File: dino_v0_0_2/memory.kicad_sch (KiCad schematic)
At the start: 10 parts, among them U19 74LS245, U21 74LS245, U24 AT28C256, U26 MCM60256AP, U51 7400

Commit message: fix(schematic): declare matching label sets so aliased nets stay one net
Three board-to-board wires were absent from the generated continuity
checklist, which is the only coverage the netlist->copper step has. A wire
missing from that list is driven by no test and sampled by no test -- the
MAR-lo post-mortem in one sentence.

Cause: cross-sheet connectivity in this design is a naming convention (all
labels are sheet-local; KiCad joins nothing between sheets). kicad_netlist
keys a net on its full label set, joined. When one sheet carries an alias and
another doesn't, the same physical wire gets two keys, both look single-sheet,
and continuity_checklist's cross-sheet filter drops the whole net.

    M15/ROM_EN   mar had both labels, memory had only ROM_EN (on a stub that
                 never joined U24.20's wire), program_counter had only M15.
                 The ROM chip-enable. Missing from every checklist ever
                 generated; survived only because a dead ~CE means the machine
                 never boots, so it self-reports.
    CW17 / CW18  microcode had the bare names, control_word had both. These
                 are U23's only wired outputs -- the entire bank-1 feature
                 rides on them, and both decoders lose their enable if either
                 is unlanded, which at the bench reads like a bad ROM burn.

Fix is in the schematic, not the tool: every sheet touching an aliased net now
declares the same label set. Alias ordering already satisfied the CWnn rule
(`~` sorts after `C`), so CW17/CW18 stay canonical and stay bus members.

  memory           U24.20  ROM_EN -> M15/ROM_EN
  program_counter  U12.9   M15    -> M15/ROM_EN
                   U14.9   M15    -> M15/ROM_EN
  microcode        U23.12  CW17   -> CW17/~{SRC_BANK}
                   U23.13  CW18   -> CW18/~{DST_BANK}

stack_pointer.kicad_sch is UUID churn only, zero connectivity change: the
sheet shipped with 14 duplicate UUIDs (one repeated 5x, consistent with the
four 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
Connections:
- net ROM_EN is gone; now on net M15: U24.20 (~{CE})
- no-connect marks 3 -> 1
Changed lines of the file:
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@@
 		(at 93.98 27.94)
-	)
-	(no_connect
-		(at 245.11 115.57)
-	)
-	(no_connect
-		(at 57.15 115.57)
 	)
 	(bus_entry
@@
 	(wire
 		(pts
+			(xy 245.11 115.57) (xy 245.11 118.11)
+		)
+		(stroke
+			(width 0)
+			(type default)
+		)
+	)
+	(wire
+		(pts
 			(xy 34.29 182.88) (xy 29.21 182.88)
 		)
@@
 		(pts
 			(xy 168.91 63.5) (xy 153.67 63.5)
+		)
+		(stroke
+			(width 0)
+			(type default)
+		)
+	)
+	(wire
+		(pts
+			(xy 57.15 115.57) (xy 57.15 118.11)
 		)
 		(stroke
@@
 		)
 	)
+	(label "ROM_EN"
+		(at 245.11 118.11 180)
+		(effects
+			(font
+				(size 1.27 1.27)
+			)
+			(justify right bottom)
+		)
+	)
 	(label "MDR7"
 		(at 148.59 76.2 180)
@@
 		)
 	)
+	(label "ROM_EN"
+		(at 57.15 118.11 0)
+		(effects
+			(font
+				(size 1.27 1.27)
+			)
+			(justify left bottom)
+		)
+	)

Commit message: feat: phase D on silicon — the machine executes from RAM
PROG_ramexec returns 0x6E. The PC has been above 0x7FFF and FETCH_RAM has
been high, both for the first time in this machine's life.

The missing condition was never "is this a fetch." ~ROM_OUT is asserted for
every src=ROM — opcode fetch, LDAI's immediate, LDA/STA/JMP/CALL operand
bytes — so an instruction living in RAM must read its operands from RAM
too. The condition is "a ROM-side read was requested, but the address is
above 0x7FFF":

    FETCH_RAM = NOR(~ROM_OUT, ~RAM_EN)

Six gate sections, no new IC. All six were free on U22/U37/U39, already in
sockets on the MDR board, where ~ROM_OUT and ~RAM_OUT already sit feeding
READS_IDLE. Only ~RAM_EN had to be brought in.

    U22 g3   FETCH_RAM     = NOR(~ROM_OUT, ~RAM_EN)
    U22 g4   ROM_BUF_ON    = NOR(~ROM_OUT, FETCH_RAM)
    U37 inv4 ~{FETCH_RAM}
    U37 inv6 ~{ROM_BUF_EN} = OR(~ROM_OUT, FETCH_RAM)   -> U19.19
    U37 inv5 ~{RAM_OE_G}   = AND(~RAM_OUT, ~FETCH_RAM) -> U26.22 + U51.9
    U39 g4   RAM_OE_ON     = NAND(~RAM_OUT, ~FETCH_RAM)

Two pin lifts on the memory board, eleven wires. U24.22 stays on ~ROM_OUT:
U24's own ~CE = M15 already deselects the ROM chip at RAM addresses.

Gating ~RAM_OUT upstream is what keeps this at six gates rather than eight.
U51 is a 7400 computing ~RAM_MDR_EN = AND(~RAM_OUT, ~WRITE_DIR), so one
gate on ~RAM_OUT moves both the RAM chip's ~OE and its buffer's ~CE.

Re-proved before building: all 15 src=ROM microcode rows carry mux_pc=True,
FETCH included, and FILL is src=NONE. A ROM-side read can now land in RAM,
so the standing "ROM reads are exempt from the src=RAM -> MAR loop" rule was
no longer free. It holds — MAR never drives M during a ROM-side read, and a
runaway opcode cannot open the loop either.

The witness is not permutation-blind. If the fetch had still come from ROM,
PC=0x9000 presents A0-A14 = 0x1000 to U24, which is 0xFF fill, which is
HALT, so the poison would have survived as 0xFF. 0x6E is 0x8B - 0x1D,
compu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
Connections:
- net ~{ROM_OUT}: no longer U19.19 (CE)
- net ~{RAM_OUT} renamed ~{RAM_OE_G}
- new net ~{ROM_BUF_EN}: U19.19 (CE)
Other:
- note added: "MODULE CONTRACT — generated, do not hand-edit (kicad_contracts.py --stamp) IN: ~{ROM_OUT} <- Control Word Module IN: ~{RAM_EN} <- Memory Address Regiser IN: M0-14, M15=ROM_EN <- Memory Address Regiser, Program Counter IN: WRITE_DIR, ~{RAM_OE_G}, ~{ROM_BUF_EN} <- Memory Data Register IN: ~{CLK} <- root OUT: MDR0-7 -> Memory Data Register, Register Modules, Stack Pointer"
- note removed: "MODULE CONTRACT — generated, do not hand-edit (kicad_contracts.py --stamp) IN: ~{RAM_OUT}, ~{ROM_OUT} <- Control Word Module IN: ~{RAM_EN} <- Memory Address Regiser IN: M0-14, M15=ROM_EN <- Memory Address Regiser, Program Counter IN: WRITE_DIR <- Memory Data Register IN: ~{CLK} <- root OUT: MDR0-7 -> Memory Data Register, Register Modules"
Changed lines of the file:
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@@
 		)
 	)
-	(text "MODULE CONTRACT — generated, do not hand-edit (kicad_contracts.py --stamp)\nIN: ~{RAM_OUT}, ~{ROM_OUT} <- Control Word Module\nIN: ~{RAM_EN} <- Memory Address Regiser\nIN: M0-14, M15=ROM_EN <- Memory Address Regiser, Program Counter\nIN: WRITE_DIR <- Memory Data Register\nIN: ~{CLK} <- root\nOUT: MDR0-7 -> Memory Data Register, Register Modules"
-		(exclude_from_sim no)
-		(at 160.02 165.1 0)
-		(effects
-			(font
-				(size 1.27 1.27)
-			)
-			(justify left bottom)
-		)
-	)
 	(text "ROM"
 		(exclude_from_sim no)
@@
 	)
 	(junction
-		(at 194.31 104.14)
-		(diameter 0)
-		(color 0 0 0 0)
-	)
-	(junction
 		(at 96.52 40.64)
 		(diameter 0)
@@
 	(wire
 		(pts
-			(xy 194.31 104.14) (xy 194.31 111.76)
-		)
-		(stroke
-			(width 0)
-			(type default)
-		)
-	)
-	(wire
-		(pts
 			(xy 109.22 83.82) (xy 104.14 83.82)
 		)
@@
 	(wire
 		(pts
-			(xy 190.5 104.14) (xy 194.31 104.14)
+			(xy 190.5 110.49) (xy 194.31 110.49)
 		)
 		(stroke
@@
 	(wire
 		(pts
-			(xy 194.31 83.82) (xy 194.31 104.14)
-		)
-		(stroke
-			(width 0)
-			(type default)
-		)
-	)
-	(wire
-		(pts
 			(xy 204.47 73.66) (xy 194.31 73.66)
 		)
@@
 		)
 	)
+	(wire
+		(pts
+			(xy 194.31 110.49) (xy 194.31 111.76)
+		)
+		(stroke
+			(width 0)
+			(type default)
+		)
+	)
 	(bus
 		(pts
@@
 	(wire
 		(pts
+			(xy 190.5 105.41) (xy 194.31 105.41)
+		)
+		(stroke
+			(width 0)
+			(type default)
+		)
+	)
+	(wire
+		(pts
 			(xy 97.79 73.66) (xy 97.79 68.58)
 		)
@@
 		)
 	)
+	(wire
+		(pts
+			(xy 194.31 83.82) (xy 194.31 105.41)
+		)
+		(stroke
+			(width 0)
+			(type default)
+		)
+	)
 	(label "M0"
 		(at 245.11 58.42 180)
@@
 		)
 	)
-	(label "~{RAM_OUT}"
+	(label "~{RAM_OE_G}"
 		(at 116.84 99.06 0)
 		(effects
@@
 	)
 	(label "~{ROM_OUT}"
-		(at 190.5 104.14 180)
+		(at 190.5 110.49 180)
 		(effects
 			(font
@@
 		)
 	)
+	(label "~{ROM_BUF_EN}"
+		(at 190.5 105.41 180)
+		(effects
+			(font
+				(size 1.27 1.27)
+			)
+			(justify right bottom)
+		)
+	)
 	(label "WRITE_DIR"
 		(at 35.56 142.24 180)
@@
 		)
 	)
-	(label "~{RAM_OUT}"
+	(label "~{RAM_OE_G}"
 		(at 29.21 182.88 180)
 		(effects
@@
 		)
 	)
+	(text "MODULE CONTRACT — generated, do not hand-edit (kicad_contracts.py --stamp)\nIN: ~{ROM_OUT} <- Control Word Module\nIN: ~{RAM_EN} <- Memory Address Regiser\nIN: M0-14, M15=ROM_EN <- Memory Address Regiser, Program Counter\nIN: WRITE_DIR, ~{RAM_OE_G}, ~{ROM_BUF_EN} <- Memory Data Register\nIN: ~{CLK} <- root\nOUT: MDR0-7 -> Memory Data Register, Register Modules, Stack Pointer"
+		(exclude_from_sim no)
+		(at 160.02 165.1 0)
+		(effects
+			(font
+				(size 1.27 1.27)
+			)
+			(justify left bottom)
+		)
+	)

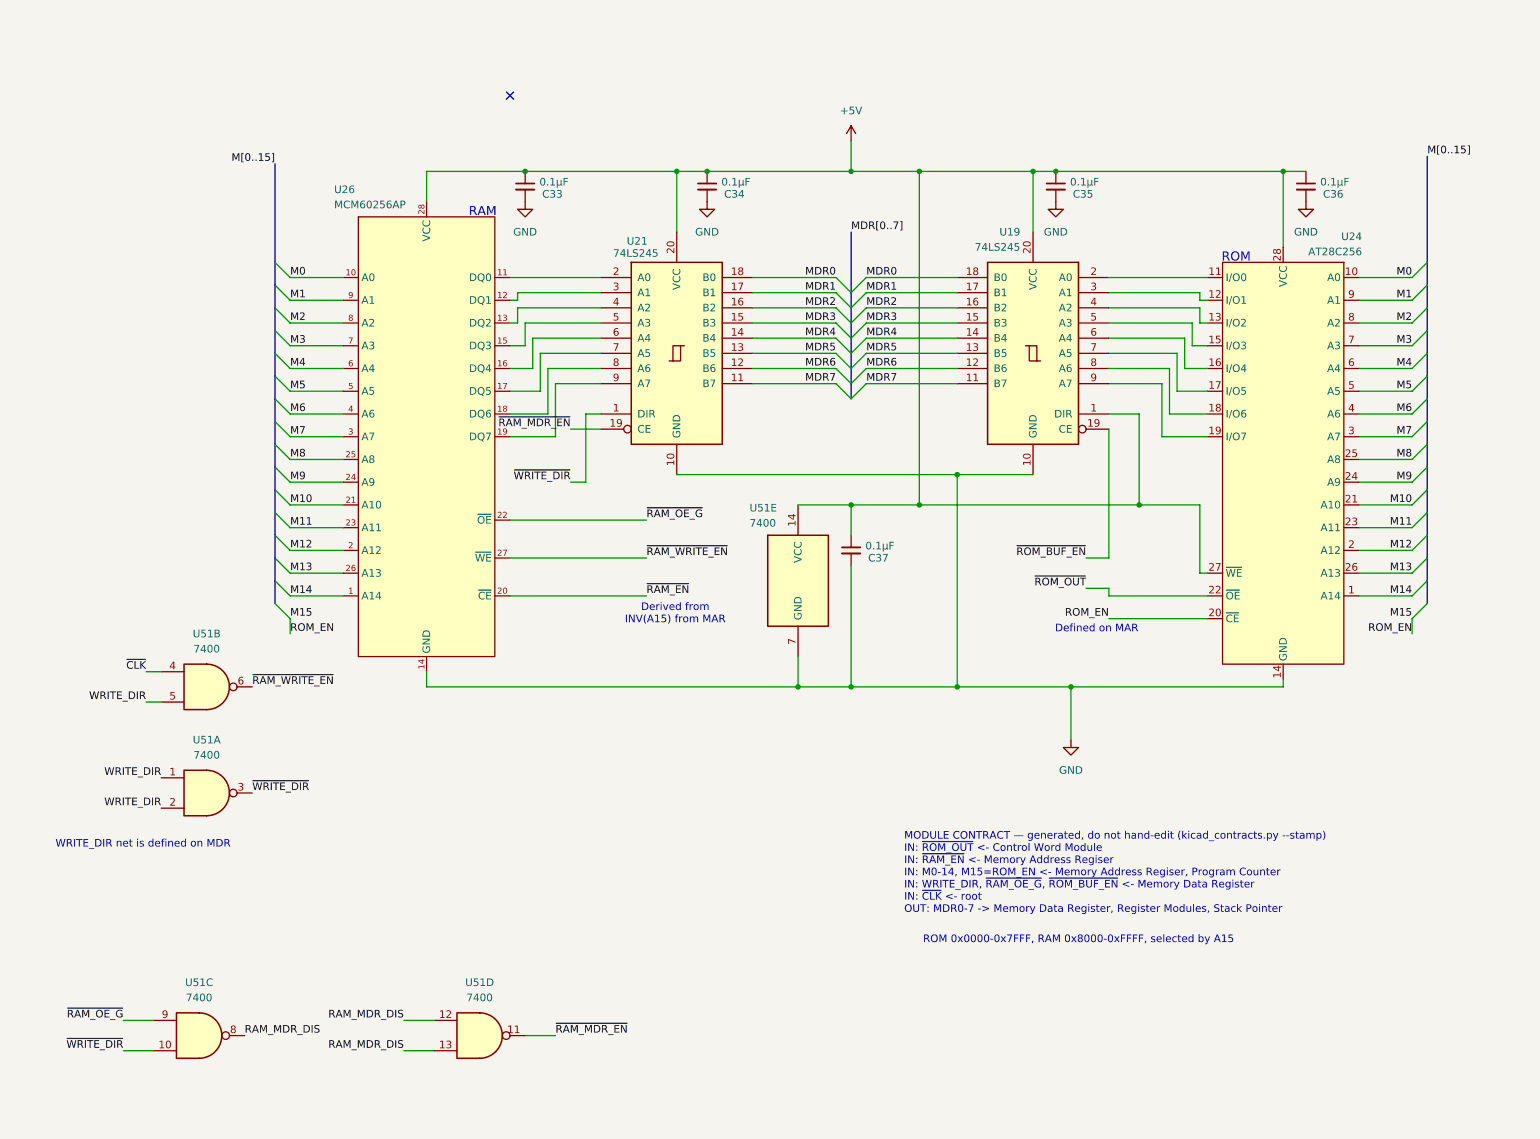
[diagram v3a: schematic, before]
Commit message: feat: phase E step A -- the 16K I/O window, in schematic
Carves 0x4000-0x7FFF out of ROM space and publishes a bus. The ROM now
answers 0x0000-0x3FFF only; the window decodes to no core chip, so W
reads its park -- 0xFF, which is HALT.

TWO NEW PACKAGES, both on the memory board:

  U74 '00  ~{M14}      = NAND(M14, M14)
           ~{ROM_SEL}  = NAND(~{RAM_EN}, ~{M14})
           ~{RAM_OE_G} = NAND(RAM_OE_ON, M15)
           ~{IO_SEL}   = NAND(~{RAM_EN}, M14)
  U75 '32  ~{IO_RD}    = OR(~{IO_SEL}, READS_IDLE)
           ~{IO_WR}    = OR(~{IO_SEL}, ~{RAM_WRITE_EN})
           RESET_B     = OR(RESET, GND)
           ~{IO_RD_Q}  = OR(~{IO_RD}, CLK)

Eight copper changes: U24.20 and U22.12 to ~{ROM_SEL}, U26.22/U51.9 fed
from U74 g3, U39.10 to ~{IO_RD}, U37.10 and U28.7 unlanded, U37.11 to
GND. Park: R4-R8 + R25-R27, 4.7k on W0-7. CLK crosses through R3, 100R,
source end -- the R2 treatment.

IN RETIRES. ~{SW_OUT} has zero pins project-wide. SWITCH-GATE1's enables
are strapped +5V until card zero drives them from an address decode.

THE ROM_EN ALIAS IS DELETED. Once U24.20 moved, ROM_EN named a net with
no ROM consumer. Deleting it half-way SPLIT the net and alias_splits()
caught it mid-edit -- M15: ['M15', 'M15/ROM_EN'], the exact two-key
failure that once cost this project the ROM chip-enable on every
continuity checklist ever generated.

CLK WAS A FOURTH CROSSING THE SPEC DID NOT CARRY. Census: 15 CLK pins,
none on the memory board; ~{CLK} at U51.4 is the wrong polarity and both
new packages are full. SECTION 1's cost table predated the read-term
split that spent U75 g4, so memory is +4 and MDR is +4 -- the wire margin
is zero. Ruled: stay on memory, the output-load argument still holds.

SWITCH-GATE1/SW1/R17-R24/C48 move to their own input.kicad_sch so the
DIP card is modelled as a card. No renumbering: 168 designators
unchanged, --since reports annotate=0.

TOOLING RECONCILED TO THE DESIGN, not the reverse:
  test_continuity_completeness  M15_PINS U24.20 -> U74.10; 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
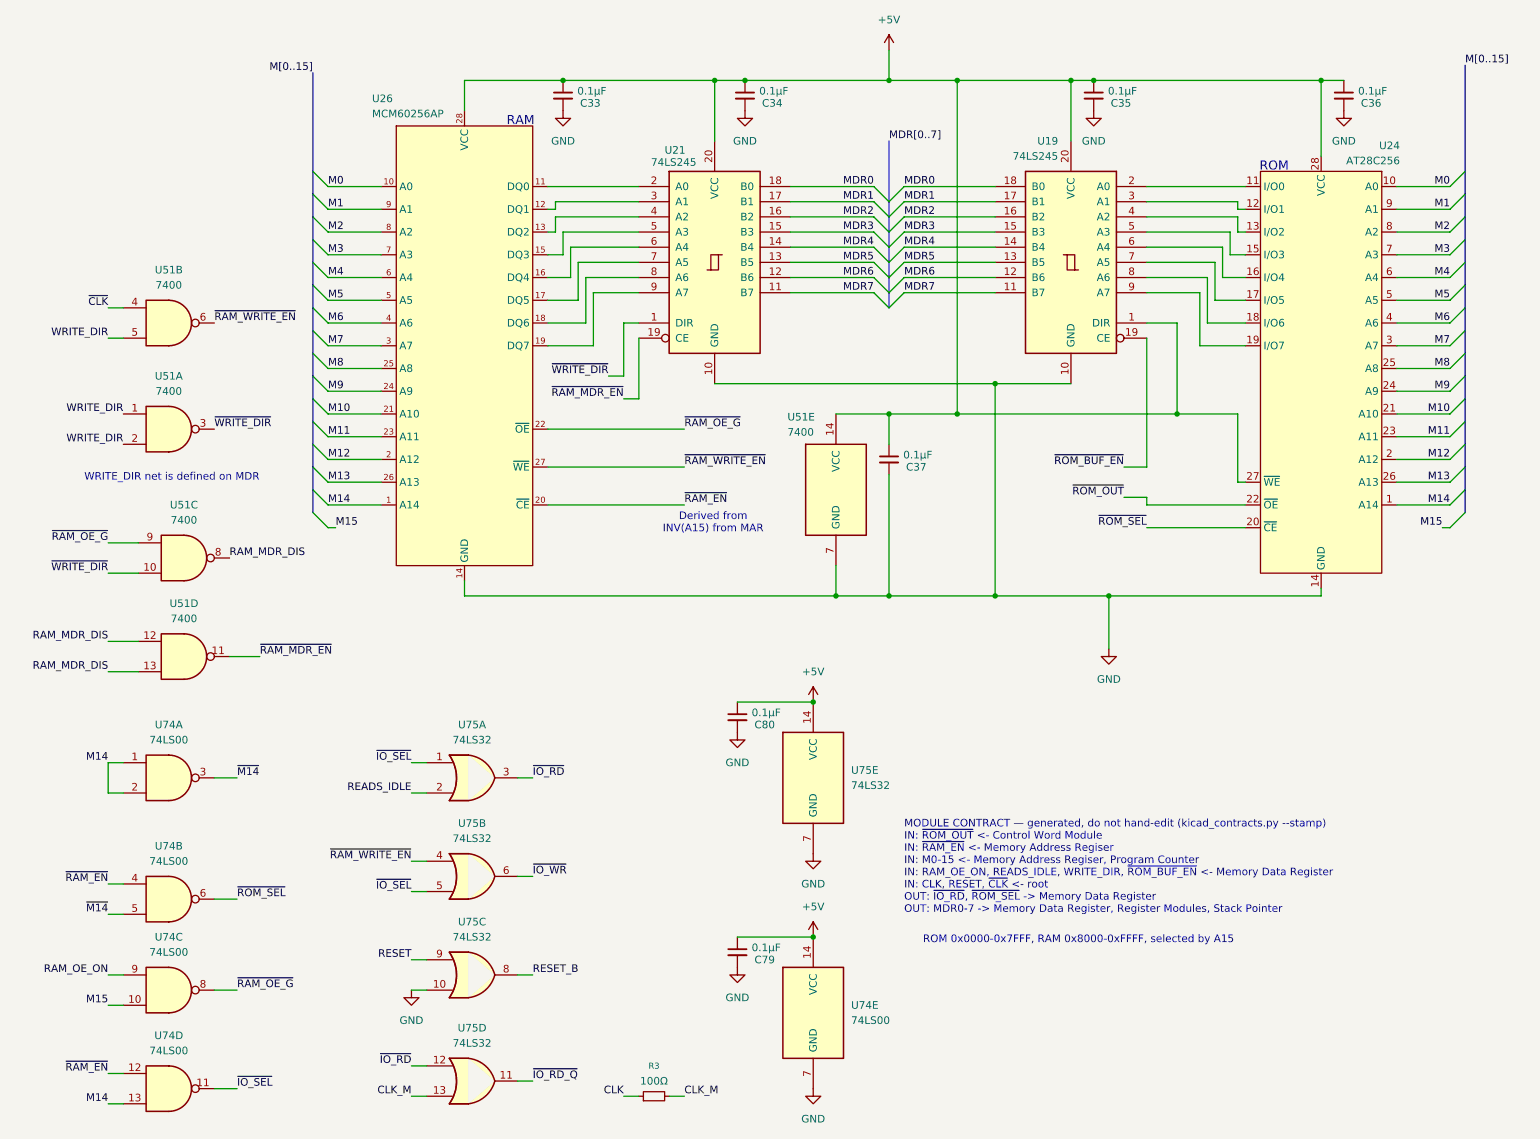
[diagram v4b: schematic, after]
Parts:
- added C79, C80: 0.1µF, symbol Device:C_Small
- added R3: 100Ω, symbol Device:R_Small
- added U74: 74LS00, symbol 74xx:74LS00
- added U75: 74LS32, symbol 74xx:74LS32
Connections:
- net +5V: now also C79.1, C80.1, U74.14 (VCC), U75.14 (VCC)
- net GND: now also C79.2, C80.2, U74.7 (GND), U75.10, U75.7 (GND)
- net M14: now also U74.1, U74.13, U74.2
- net M15: now also U74.10; no longer U24.20 (~{CE})
- net ~{RAM_EN}: now also U74.12, U74.4
- net ~{RAM_OE_G}: now also U74.8
- net ~{RAM_WRITE_EN}: now also U75.4
- new net CLK: R3.1
- new net CLK_M: R3.2, U75.13
- new net RAM_OE_ON: U74.9
- new net READS_IDLE: U75.2
- new net RESET: U75.9
- new net RESET_B: U75.8
- new net ~{IO_RD_Q}: U75.11
- new net ~{IO_RD}: U75.12, U75.3
- new net ~{IO_SEL}: U74.11, U75.1, U75.5
- new net ~{IO_WR}: U75.6
- new net ~{M14}: U74.3, U74.5
- new net ~{ROM_SEL}: U24.20 (~{CE}), U74.6
- no-connect marks 1 -> 0
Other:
- note added: "MODULE CONTRACT — generated, do not hand-edit (kicad_contracts.py --stamp) IN: ~{ROM_OUT} <- Control Word Module IN: ~{RAM_EN} <- Memory Address Regiser IN: M0-15 <- Memory Address Regiser, Program Counter IN: RAM_OE_ON, READS_IDLE, WRITE_DIR, ~{ROM_BUF_EN} <- Memory Data Register IN: CLK, RESET, ~{CLK} <- root OUT: ~{IO_RD}, ~{ROM_SEL} -> Memory Data Register OUT: MDR0-7 -> Memory Data Register,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"
- note removed: "Defined on MAR"
- note removed: "MODULE CONTRACT — generated, do not hand-edit (kicad_contracts.py --stamp) IN: ~{ROM_OUT} <- Control Word Module IN: ~{RAM_EN} <- Memory Address Regiser IN: M0-14, M15=ROM_EN <- Memory Address Regiser, Program Counter IN: WRITE_DIR, ~{RAM_OE_G}, ~{ROM_BUF_EN} <- Memory Data Register IN: ~{CLK} <- root OUT: MDR0-7 -> Memory Data Register, Register Modules, Stack Pointer"
- moved on the sheet: C33, C34, C35, C36, C37, U19, U21, U24, U26, U51A, U51B, U51C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
